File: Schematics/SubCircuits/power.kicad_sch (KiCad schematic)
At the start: 9 parts, among them J4 Batt_alt, SW1 PHB2UOATS1A, U2 TPS63001

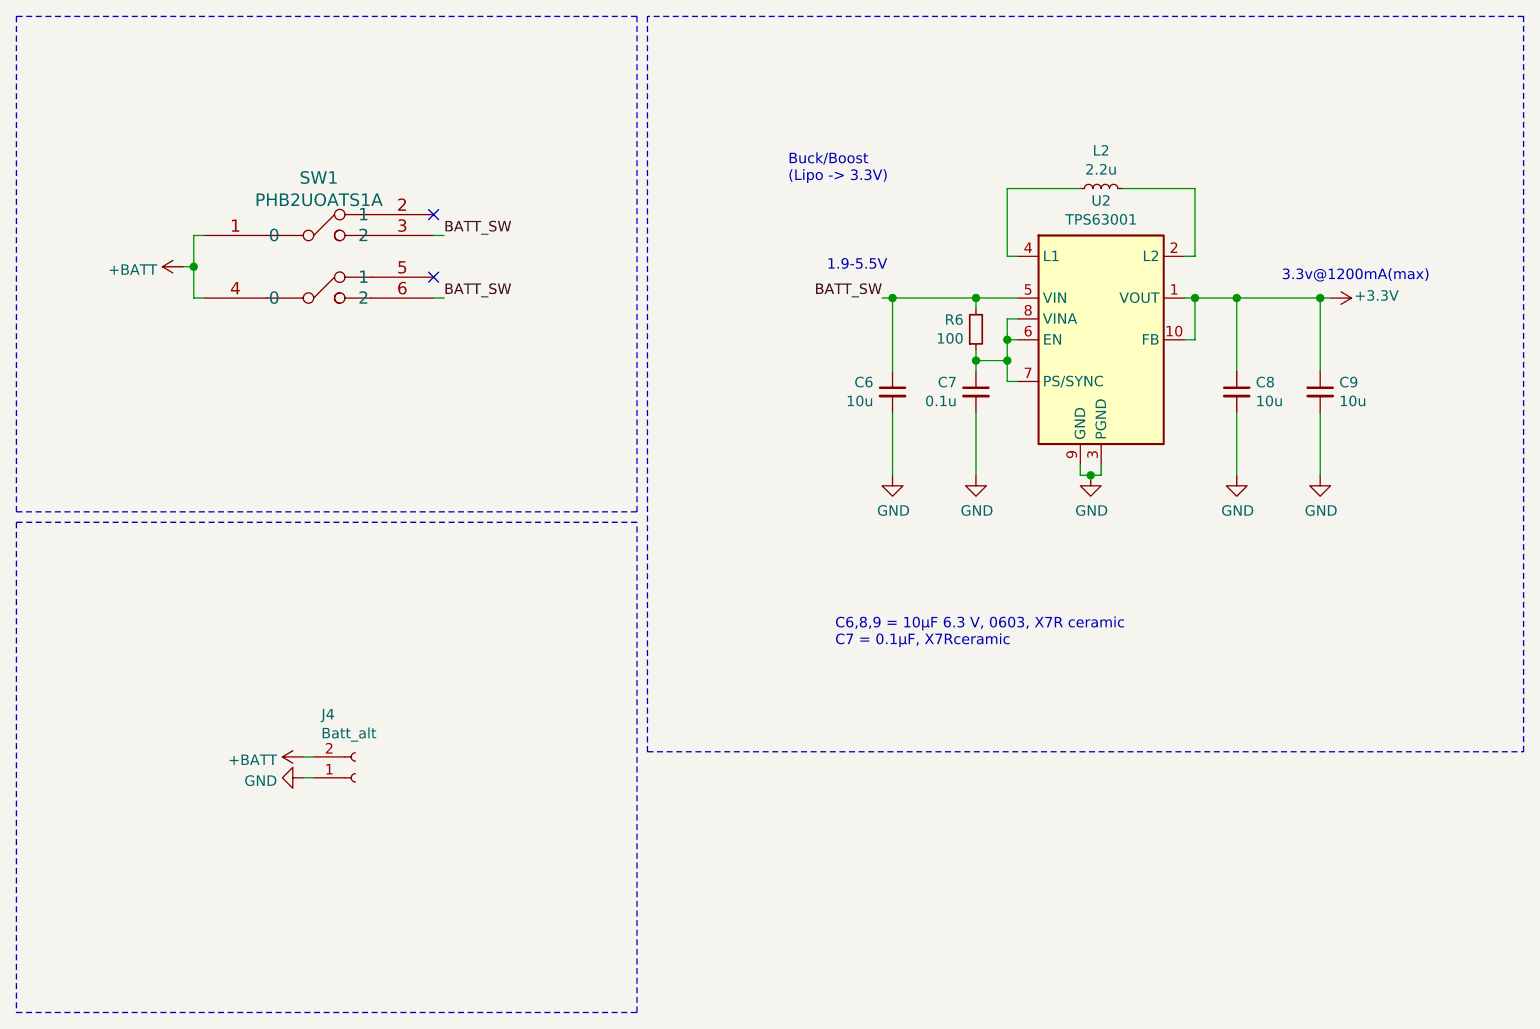
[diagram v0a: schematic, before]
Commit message: Added defunct subcircuit project
superseded by modular mainboard
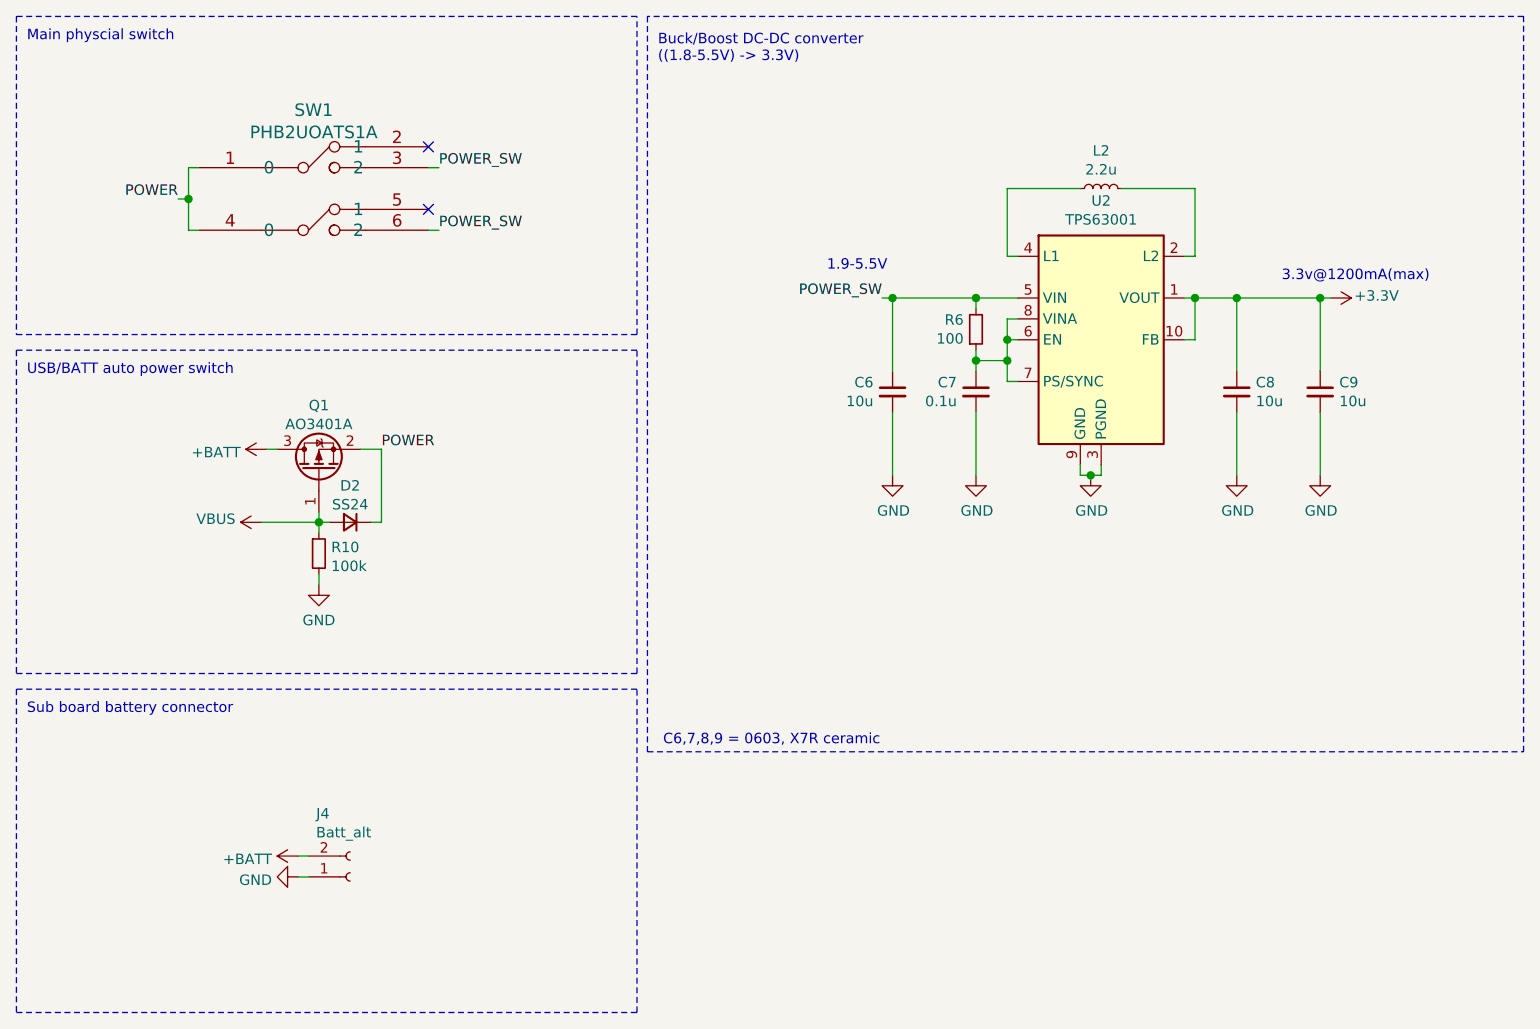
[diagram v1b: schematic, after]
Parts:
- added D2: SS24, Diode_SMD:D_SMA, symbol Device:D_Small
- added Q1: AO3401A, Package_TO_SOT_SMD:SOT-23, symbol Transistor_FET:AO3401A
- added R10: 100k, Resistor_SMD:R_0603_1608Metric, symbol Device:R_Small
- U2: LCSC Part C28060 -> (none)
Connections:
- net +BATT: now also Q1.3 (D); no longer SW1.1 (0), SW1.4 (0)
- net GND: now also R10.2
- net BATT_SW renamed POWER_SW
- new net POWER: D2.1 (K), Q1.2 (S), SW1.1 (0), SW1.4 (0)
- new net VBUS: D2.2 (A), Q1.1 (G), R10.1
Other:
- note added: "Buck/Boost DC-DC converter ((1.8-5.5V) -> 3.3V)"
- note added: "C6,7,8,9 = 0603, X7R ceramic"
- note added: "Main physcial switch"
- note added: "Sub board battery connector"
- note added: "USB/BATT auto power switch"
- note removed: "Buck/Boost (Lipo -> 3.3V)"
- note removed: "C6,8,9 = 10μF 6.3 V, 0603, X7R ceramic C7 = 0.1μF, X7Rceramic"
- moved on the sheet: J4, SW1
